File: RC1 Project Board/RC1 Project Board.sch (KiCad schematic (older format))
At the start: 20 parts, among them J1 Signals, J3 SBC, J4 ADDRESS, J5 Port A, J6 Port B, J7 PWR1, J8 PWR2, M1 Mounting, M2 Mounting, M3 Mounting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

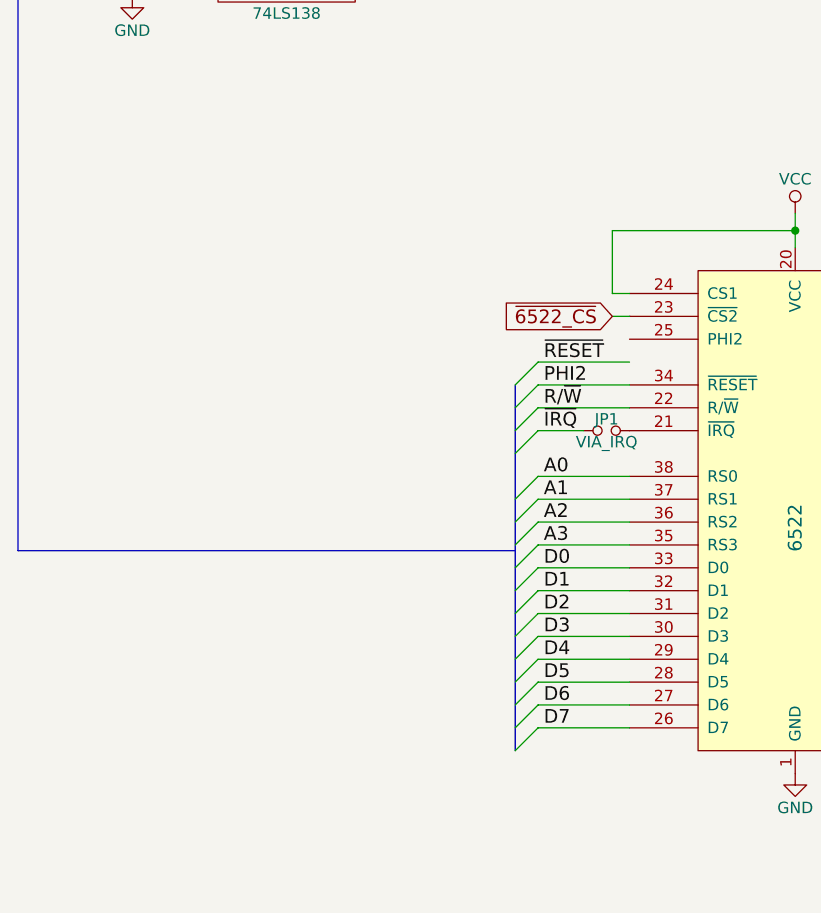
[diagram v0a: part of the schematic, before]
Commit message: Project board has clock select pins
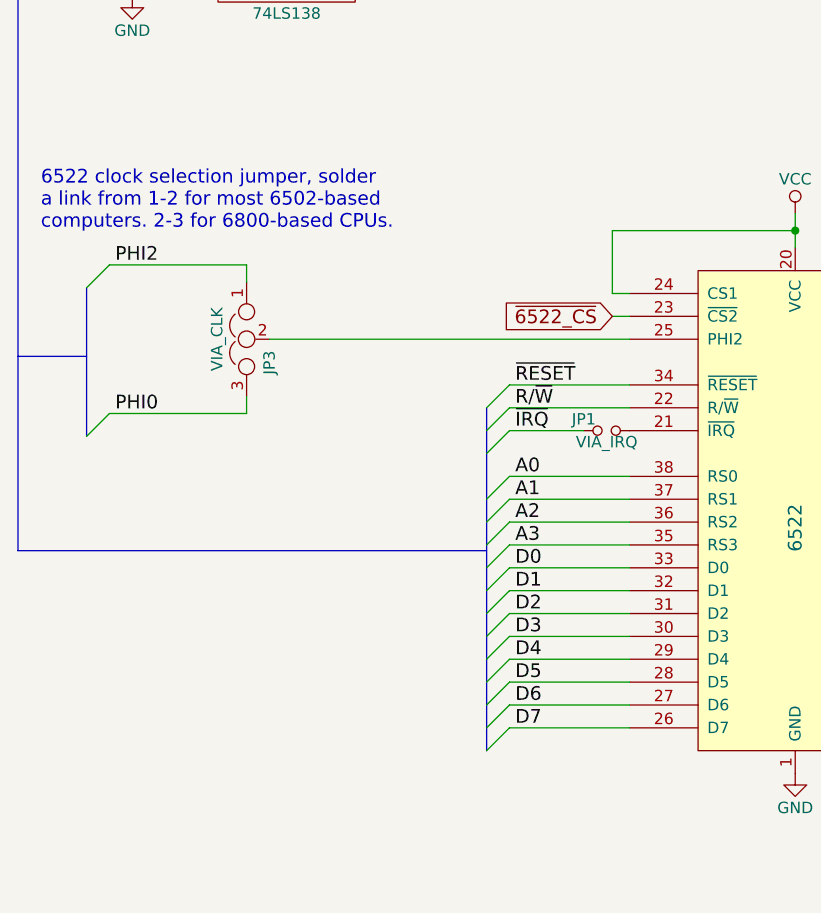
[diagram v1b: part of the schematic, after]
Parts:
- added JP3: VIA_CLK, Pin_Headers:Pin_Header_Straight_1x03_Pitch2.54mm, symbol Jumper_NC_Dual
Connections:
- net PHI0: now also JP3.3
- net PHI2: now also JP3.1; no longer U2.34 (~RESET)
- net ~IRQ: now also JP1.1; no longer JP1.2
- net ~RESET: now also U2.34 (~RESET)
- net at U2.21 (~IRQ): now also JP1.2; no longer JP1.1
- net at U2.25 (PHI2): now also JP3.2
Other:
- note added: "6522 clock selection jumper, solder\na link from 1-2 for most 6502-based\ncomputers. 2-3 for 6800-based CPUs."
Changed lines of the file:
@@
 	10400 3000 10500 3100
 $Comp
-L VCC #PWR05
+L VCC #PWR03
 U 1 1 5DD0D2FE
 P 10275 4575
-F 0 "#PWR05" H 10275 4425 50  0001 C CNN
+F 0 "#PWR03" H 10275 4425 50  0001 C CNN
 F 1 "VCC" H 10275 4725 50  0000 C CNN
 F 2 "" H 10275 4575 50  0001 C CNN
@@
 $EndComp
 $Comp
-L GND #PWR06
+L GND #PWR04
 U 1 1 5DD0D304
 P 10200 4775
-F 0 "#PWR06" H 10200 4525 50  0001 C CNN
+F 0 "#PWR04" H 10200 4525 50  0001 C CNN
 F 1 "GND" H 10200 4625 50  0000 C CNN
 F 2 "" H 10200 4775 50  0001 C CNN
@@
 	11525 10650 11525 10800
 $Comp
-L GND #PWR07
+L GND #PWR05
 U 1 1 5DD0E2DE
 P 11525 10800
-F 0 "#PWR07" H 11525 10550 50  0001 C CNN
+F 0 "#PWR05" H 11525 10550 50  0001 C CNN
 F 1 "GND" H 11525 10650 50  0000 C CNN
 F 2 "" H 11525 10800 50  0001 C CNN
@@
 Connection ~ 11250 10725
 $Comp
-L VCC #PWR08
+L VCC #PWR06
 U 1 1 5DD0E425
 P 10975 10300
-F 0 "#PWR08" H 10975 10150 50  0001 C CNN
+F 0 "#PWR06" H 10975 10150 50  0001 C CNN
 F 1 "VCC" H 10975 10450 50  0000 C CNN
 F 2 "" H 10975 10300 50  0001 C CNN
@@
 $EndComp
 $Comp
-L VCC #PWR09
+L VCC #PWR07
 U 1 1 5DE70879
 P 4150 4025
-F 0 "#PWR09" H 4150 3875 50  0001 C CNN
+F 0 "#PWR07" H 4150 3875 50  0001 C CNN
 F 1 "VCC" H 4150 4175 50  0000 C CNN
 F 2 "" H 4150 4025 50  0001 C CNN
@@
 $EndComp
 $Comp
-L GND #PWR010
+L GND #PWR08
 U 1 1 5DE70A6F
 P 4150 6475
-F 0 "#PWR010" H 4150 6225 50  0001 C CNN
+F 0 "#PWR08" H 4150 6225 50  0001 C CNN
 F 1 "GND" H 4150 6325 50  0000 C CNN
 F 2 "" H 4150 6475 50  0001 C CNN
@@
 	-1   0    0    -1
 $EndComp
-Text Label 3050 5475 0    60   ~ 0
+Text Label 2925 5475 0    60   ~ 0
 A3
-Text Label 3050 5375 0    60   ~ 0
+Text Label 2925 5375 0    60   ~ 0
 A2
-Text Label 3050 5275 0    60   ~ 0
+Text Label 2925 5275 0    60   ~ 0
 A1
-Text Label 3050 5175 0    60   ~ 0
+Text Label 2925 5175 0    60   ~ 0
 A0
 Wire Wire Line
-	3425 5275 3025 5275
-Wire Wire Line
-	3425 5375 3025 5375
-Wire Wire Line
-	3425 5475 3025 5475
-Wire Wire Line
-	3425 5175 3025 5175
-Text Label 3050 4675 0    60   ~ 0
+	2900 5275 3425 5275
+Wire Wire Line
+	2900 5375 3425 5375
+Wire Wire Line
+	2900 5475 3425 5475
+Wire Wire Line
+	2900 5175 3425 5175
+Text Label 2925 4775 0    60   ~ 0
 ~RESET
-Text Label 3050 6275 0    60   ~ 0
+Text Label 2925 6275 0    60   ~ 0
 D7
-Text Label 3050 6175 0    60   ~ 0
+Text Label 2925 6175 0    60   ~ 0
 D6
-Text Label 3050 6075 0    60   ~ 0
+Text Label 2925 6075 0    60   ~ 0
 D5
-Text Label 3050 5975 0    60   ~ 0
+Text Label 2925 5975 0    60   ~ 0
 D4
-Text Label 3050 5875 0    60   ~ 0
+Text Label 2925 5875 0    60   ~ 0
 D3
-Text Label 3050 5775 0    60   ~ 0
+Text Label 2925 5775 0    60   ~ 0
 D2
-Text Label 3050 5675 0    60   ~ 0
+Text Label 2925 5675 0    60   ~ 0
 D1
-Text Label 3050 5575 0    60   ~ 0
+Text Label 2925 5575 0    60   ~ 0
 D0
 Wire Wire Line
-	3425 6275 3025 6275
-Wire Wire Line
-	3425 6175 3025 6175
-Wire Wire Line
-	3425 6075 3025 6075
-Wire Wire Line
-	3425 5975 3025 5975
-Wire Wire Line
-	3425 5875 3025 5875
-Wire Wire Line
-	3425 5775 3025 5775
-Wire Wire Line
-	3425 5675 3025 5675
-Wire Wire Line
-	3425 5575 3025 5575
-Wire Wire Line
-	3425 4675 3025 4675
-Wire Wire Line
-	3425 4775 3025 4775
-Text Label 3050 4775 0    60   ~ 0
+	2900 6275 3425 6275
+Wire Wire Line
+	2900 6175 3425 6175
+Wire Wire Line
+	2900 6075 3425 6075
+Wire Wire Line
+	2900 5975 3425 5975
+Wire Wire Line
+	2900 5875 3425 5875
+Wire Wire Line
+	2900 5775 3425 5775
+Wire Wire Line
+	2900 5675 3425 5675
+Wire Wire Line
+	2900 5575 3425 5575
+Wire Wire Line
+	2900 4775 3425 4775
+Text Label 1175 4250 0    60   ~ 0
 PHI2
-Text Label 3050 4875 0    60   ~ 0
+Text Label 2925 4875 0    60   ~ 0
 R/~W
 Wire Wire Line
-	3025 4875 3425 4875
+	2900 4875 3425 4875
 $Comp
 L Jumper_NO_Small JP1
 U 1 1 5DE720C4
 P 3325 4975
-F 0 "JP1" H 3325 5025 50  0000 C CNN
+F 0 "JP1" H 3225 5025 50  0000 C CNN
 F 1 "VIA_IRQ" H 3325 4925 50  0000 C CNN
 F 2 "Pin_Headers:Pin_Header_Straight_1x02_Pitch2.54mm" H 3325 4975 50  0001 C CNN
 F 3 "" H 3325 4975 50  0001 C CNN
 	1    3325 4975
-	-1   0    0    -1
-$EndComp
-Text Label 3050 4975 0    60   ~ 0
+	1    0    0    -1
+$EndComp
+Text Label 2925 4975 0    60   ~ 0
 ~IRQ
 Wire Wire Line
-	3025 4975 3225 4975
-Entry Wire Line
-	3025 4675 2925 4775
-Entry Wire Line
-	3025 4775 2925 4875
-Entry Wire Line
-	3025 4875 2925 4975
-Entry Wire Line
-	3025 4975 2925 5075
-Entry Wire Line
-	3025 5175 2925 5275
-Entry Wire Line
-	3025 5275 2925 5375
-Entry Wire Line
-	3025 5375 2925 5475
-Entry Wire Line
-	3025 5475 2925 5575
-Entry Wire Line
-	3025 5575 2925 5675
-Entry Wire Line
-	3025 5675 2925 5775
-Entry Wire Line
-	3025 5775 2925 5875
-Entry Wire Line
-	3025 5875 2925 5975
-Entry Wire Line
-	3025 5975 2925 6075
-Entry Wire Line
-	3025 6075 2925 6175
-Entry Wire Line
-	3025 6175 2925 6275
-Entry Wire Line
-	3025 6275 2925 6375
+	2900 4975 3225 4975
+Entry Wire Line
+	2900 4775 2800 4875
+Entry Wire Line
+	2900 4875 2800 4975
+Entry Wire Line
+	2900 4975 2800 5075
+Entry Wire Line
+	2900 5175 2800 5275
+Entry Wire Line
+	2900 5275 2800 5375
+Entry Wire Line
+	2900 5375 2800 5475
+Entry Wire Line
+	2900 5475 2800 5575
+Entry Wire Line
+	2900 5575 2800 5675
+Entry Wire Line
+	2900 5675 2800 5775
+Entry Wire Line
+	2900 5775 2800 5875
+Entry Wire Line
+	2900 5875 2800 5975
+Entry Wire Line
+	2900 5975 2800 6075
+Entry Wire Line
+	2900 6075 2800 6175
+Entry Wire Line
+	2900 6175 2800 6275
+Entry Wire Line
+	2900 6275 2800 6375
 Text Label 14700 6800 2    60   ~ 0
 ~IO3
@@
 	5025 6475 5325 6475
 Wire Bus Line
-	2925 4775 2925 6375
+	2800 4875 2800 6375
 $Comp
 L 74LS138 U1
@@
 A14
 $Comp
-L GND #PWR011
+L GND #PWR09
 U 1 1 5DE7616F
 P 1250 3075
-F 0 "#PWR011" H 1250 2825 50  0001 C CNN
+F 0 "#PWR09" H 1250 2825 50  0001 C CNN
 F 1 "GND" H 1250 2925 50  0000 C CNN
 F 2 "" H 1250 3075 50  0001 C CNN
@@
 NoConn ~ 5900 2500
 $Comp
-L GND #PWR012
+L GND #PWR010
 U 1 1 5DE76176
 P 4625 2675
-F 0 "#PWR012" H 4625 2425 50  0001 C CNN
+F 0 "#PWR010" H 4625 2425 50  0001 C CNN
 F 1 "GND" H 4625 2525 50  0000 C CNN
 F 2 "" H 4625 2675 50  0001 C CNN
@@
 	4100 1900 4200 1900
 $Comp
-L VCC #PWR013
+L VCC #PWR011
 U 1 1 5DE7619F
 P 4625 2325
-F 0 "#PWR013" H 4625 2175 50  0001 C CNN
+F 0 "#PWR011" H 4625 2175 50  0001 C CNN
 F 1 "VCC" H 4625 2475 50  0000 C CNN
 F 2 "" H 4625 2325 50  0001 C CNN
@@
 	7400 2650 7400 875
 Wire Bus Line
-	750  5500 2925 5500
+	750  5500 2800 5500
 $Comp
 L Conn_01x02 J7
@@
 $EndComp
 $Comp
-L VCC #PWR014
+L VCC #PWR012
 U 1 1 5DE7B0A8
 P 7625 4800
-F 0 "#PWR014" H 7625 4650 50  0001 C CNN
+F 0 "#PWR012" H 7625 4650 50  0001 C CNN
 F 1 "VCC" H 7625 4950 50  0000 C CNN
 F 2 "" H 7625 4800 50  0001 C CNN
@@
 	7625 4975 7625 5050
 $Comp
-L GND #PWR015
+L GND #PWR013
 U 1 1 5DE7B331
 P 7625 5050
-F 0 "#PWR015" H 7625 4800 50  0001 C CNN
+F 0 "#PWR013" H 7625 4800 50  0001 C CNN
 F 1 "GND" H 7625 4900 50  0000 C CNN
 F 2 "" H 7625 5050 50  0001 C CNN
@@
 $EndComp
 $Comp
-L VCC #PWR016
+L VCC #PWR014
 U 1 1 5DE7B3E8
 P 7625 5550
-F 0 "#PWR016" H 7625 5400 50  0001 C CNN
+F 0 "#PWR014" H 7625 5400 50  0001 C CNN
 F 1 "VCC" H 7625 5700 50  0000 C CNN
 F 2 "" H 7625 5550 50  0001 C CNN
@@
 	7625 5725 7625 5800
 $Comp
-L GND #PWR017
+L GND #PWR015
 U 1 1 5DE7B3F2
 P 7625 5800
-F 0 "#PWR017" H 7625 5550 50  0001 C CNN
+F 0 "#PWR015" H 7625 5550 50  0001 C CNN
 F 1 "GND" H 7625 5650 50  0000 C CNN
 F 2 "" H 7625 5800 50  0001 C CNN
@@
 Wire Wire Line
 	3350 4475 3425 4475
+Wire Wire Line
+	1850 4575 3425 4575
+$Comp
+L Jumper_NC_Dual JP3
+U 1 1 5E02AB75
+P 1750 4575
+F 0 "JP3" H 1800 4475 50  0000 L CNN
+F 1 "VIA_CLK" H 1750 4675 50  0000 C BNN
+F 2 "Pin_Headers:Pin_Header_Straight_1x03_Pitch2.54mm" H 1750 4575 50  0001 C CNN
+F 3 "" H 1750 4575 50  0001 C CNN
+	1    1750 4575
+	0    -1   1    0
+$EndComp
+Wire Wire Line
+	1750 4250 1750 4325
+Wire Wire Line
+	1150 4250 1750 4250
+Wire Wire Line
+	1750 4900 1750 4825
+Entry Wire Line
+	1150 4250 1050 4350
+Wire Wire Line
+	1150 4900 1750 4900
+Entry Wire Line
+	1150 4900 1050 5000
+Text Label 1175 4900 0    60   ~ 0
+PHI0
+Wire Bus Line
+	1050 5000 1050 4350
+Wire Bus Line
+	750  4650 1050 4650
+Text Notes 850  4100 0    60   ~ 0
+6522 clock selection jumper, solder\na link from 1-2 for most 6502-based\ncomputers. 2-3 for 6800-based CPUs.
 $EndSCHEMATC
